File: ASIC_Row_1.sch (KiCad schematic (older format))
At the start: 60 parts, among them U14 BITFURY, U15 BITFURY, U16 BITFURY, U17 BITFURY, U18 BITFURY

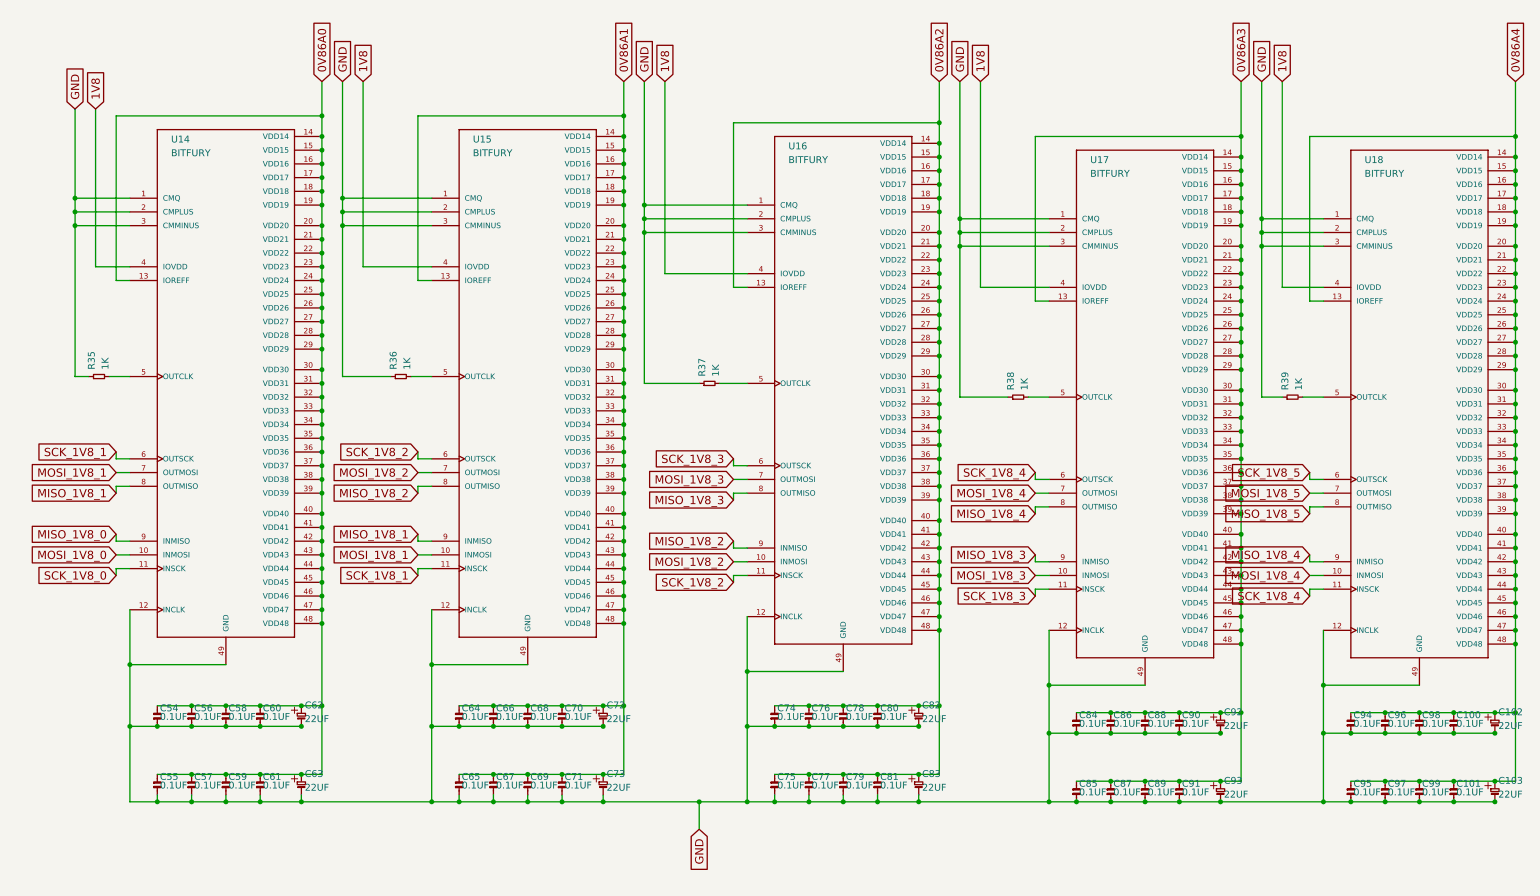
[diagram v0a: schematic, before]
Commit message: Fixed schematic wiring mismatch. initial layout and wiring
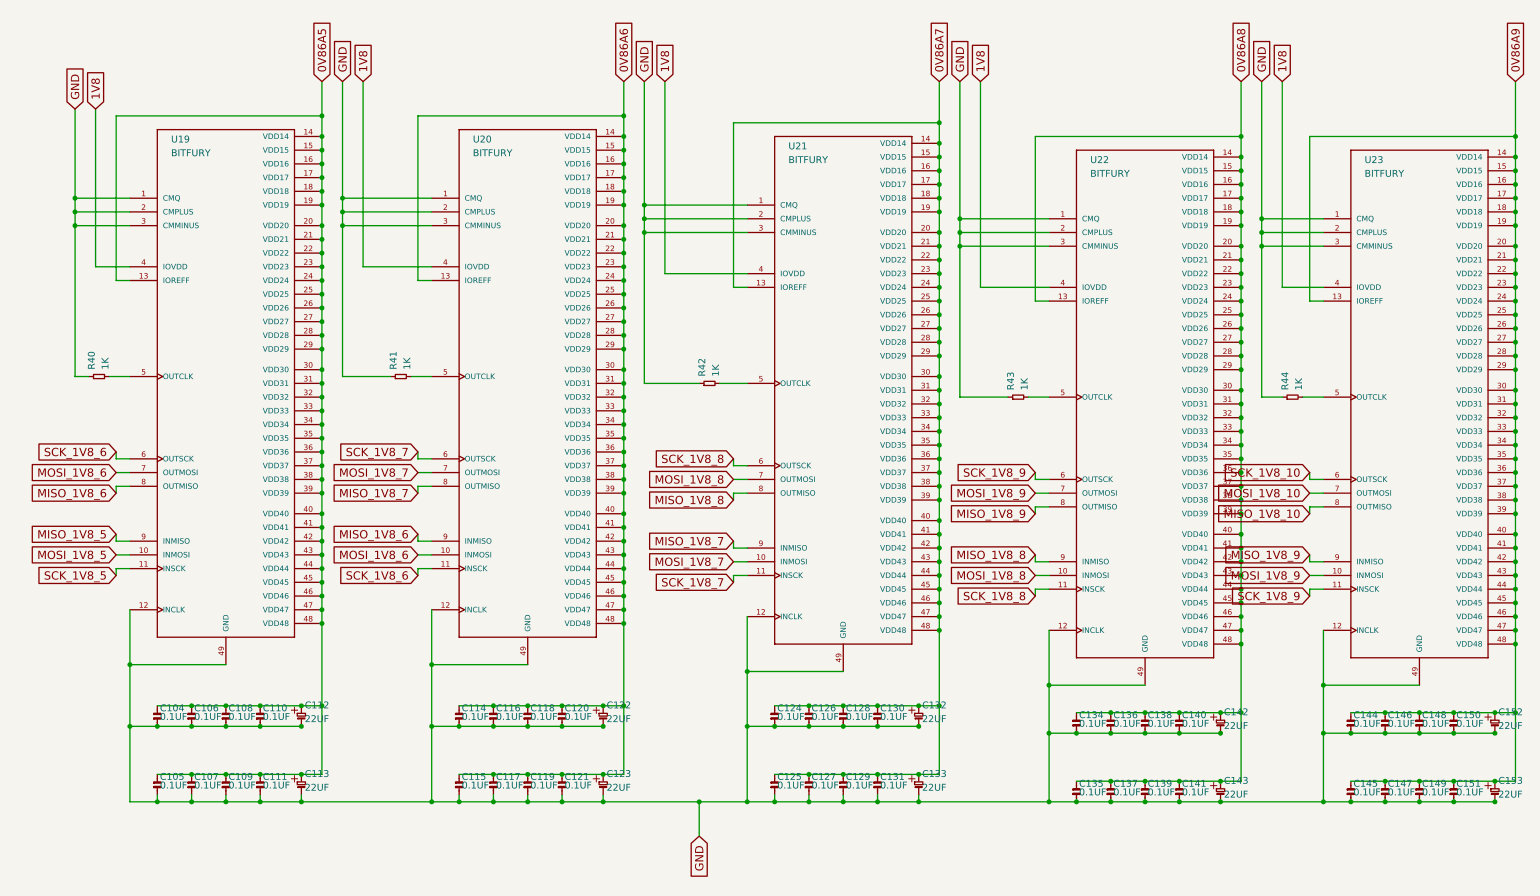
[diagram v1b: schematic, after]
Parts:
- removed C100, C101, C54, C55, C56, C57, C58, C59, C60, C61, C64, C65, C66, C67, C68, C69, C70, C71, C74, C75, C76, C77, C78, C79, C80, C81, C84, C85, C86, C87, C88, C89, C90, C91, C94, C95, C96, C97, C98, C99: 0.1UF, symbol CAPACITOR-NONPOLAR
- removed C102, C103, C62, C63, C72, C73, C82, C83, C92, C93: 22UF, ~, symbol CAPACITOR-POLAR
- removed R35, R36, R37, R38, R39: 1K, symbol RESISTOR
- removed U14, U15, U16, U17, U18: BITFURY, bitfury-QFN48, symbol BITFURY
- added C104, C105, C106, C107, C108, C109, C110, C111, C114, C115, C116, C117, C118, C119, C120, C121, C124, C125, C126, C127, C128, C129, C130, C131, C134, C135, C136, C137, C138, C139, C140, C141, C144, C145, C146, C147, C148, C149, C150, C151: 0.1UF, symbol CAPACITOR-NONPOLAR
- added C112, C113, C122, C123, C132, C133, C142, C143, C152, C153: 22UF, ~, symbol CAPACITOR-POLAR
- added R40, R41, R42, R43, R44: 1K, symbol RESISTOR
- added U19, U20, U21, U22, U23: BITFURY, bitfury-QFN48, symbol BITFURY
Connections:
- net 1V8: now also U19.4 (IOVDD), U20.4 (IOVDD), U21.4 (IOVDD), U22.4 (IOVDD), U23.4 (IOVDD)
- net GND: now also C104.2, C105.2, C106.2, C107.2, C108.2, C109.2, C110.2, C111.2, C112.2, C113.2, C114.2, C115.2, C116.2, C117.2, C118.2, C119.2, C120.2, C121.2, C122.2, C123.2, C124.2, C125.2, C126.2, C127.2, C128.2, C129.2, C130.2, C131.2, C132.2, C133.2, C134.2, C135.2, C136.2, C137.2, C138.2, C139.2, C140.2, C141.2, C142.2, C143.2, C144.2, C145.2, C146.2, C147.2, C148.2, C149.2, C150.2, C151.2, C152.2, C153.2, R40.2, R41.2, R42.2, R43.2, R44.2, U19.1 (CMQ), U19.12 (INCLK), U19.2 (CMPLUS), U19.3 (CMMINUS), U19.49 (GND), U20.1 (CMQ), U20.12 (INCLK), U20.2 (CMPLUS), U20.3 (CMMINUS), U20.49 (GND), U21.1 (CMQ), U21.12 (INCLK), U21.2 (CMPLUS), U21.3 (CMMINUS), U21.49 (GND), U22.1 (CMQ), U22.12 (INCLK), U22.2 (CMPLUS), U22.3 (CMMINUS), U22.49 (GND), U23.1 (CMQ), U23.12 (INCLK), U23.2 (CMPLUS), U23.3 (CMMINUS), U23.49 (GND)
- net MISO_1V8_5: now also U19.9 (INMISO)
- net MOSI_1V8_5: now also U19.10 (INMOSI)
- net SCK_1V8_5: now also U19.11 (INSCK)
- new net: R40.1, U19.5 (OUTCLK)
- new net: R43.1, U22.5 (OUTCLK)
- new net: R44.1, U23.5 (OUTCLK)
- new net: R41.1, U20.5 (OUTCLK)
- new net: R42.1, U21.5 (OUTCLK)
- new net 0V86A5: C104.1, C105.1, C106.1, C107.1, C108.1, C109.1, C110.1, C111.1, C112.1, C113.1, U19.13 (IOREFF), U19.14 (VDD14), U19.15 (VDD15), U19.16 (VDD16), U19.17 (VDD17), U19.18 (VDD18), U19.19 (VDD19), U19.20 (VDD20), U19.21 (VDD21), U19.22 (VDD22), U19.23 (VDD23), U19.24 (VDD24), U19.25 (VDD25), U19.26 (VDD26), U19.27 (VDD27), U19.28 (VDD28), U19.29 (VDD29), U19.30 (VDD30), U19.31 (VDD31), U19.32 (VDD32), U19.33 (VDD33), U19.34 (VDD34), U19.35 (VDD35), U19.36 (VDD36), U19.37 (VDD37), U19.38 (VDD38), U19.39 (VDD39), U19.40 (VDD40), U19.41 (VDD41), U19.42 (VDD42), U19.43 (VDD43), U19.44 (VDD44), U19.45 (VDD45), U19.46 (VDD46), U19.47 (VDD47), U19.48 (VDD48)
- new net 0V86A6: C114.1, C115.1, C116.1, C117.1, C118.1, C119.1, C120.1, C121.1, C122.1, C123.1, U20.13 (IOREFF), U20.14 (VDD14), U20.15 (VDD15), U20.16 (VDD16), U20.17 (VDD17), U20.18 (VDD18), U20.19 (VDD19), U20.20 (VDD20), U20.21 (VDD21), U20.22 (VDD22), U20.23 (VDD23), U20.24 (VDD24), U20.25 (VDD25), U20.26 (VDD26), U20.27 (VDD27), U20.28 (VDD28), U20.29 (VDD29), U20.30 (VDD30), U20.31 (VDD31), U20.32 (VDD32), U20.33 (VDD33), U20.34 (VDD34), U20.35 (VDD35), U20.36 (VDD36), U20.37 (VDD37), U20.38 (VDD38), U20.39 (VDD39), U20.40 (VDD40), U20.41 (VDD41), U20.42 (VDD42), U20.43 (VDD43), U20.44 (VDD44), U20.45 (VDD45), U20.46 (VDD46), U20.47 (VDD47), U20.48 (VDD48)
- new net 0V86A7: C124.1, C125.1, C126.1, C127.1, C128.1, C129.1, C130.1, C131.1, C132.1, C133.1, U21.13 (IOREFF), U21.14 (VDD14), U21.15 (VDD15), U21.16 (VDD16), U21.17 (VDD17), U21.18 (VDD18), U21.19 (VDD19), U21.20 (VDD20), U21.21 (VDD21), U21.22 (VDD22), U21.23 (VDD23), U21.24 (VDD24), U21.25 (VDD25), U21.26 (VDD26), U21.27 (VDD27), U21.28 (VDD28), U21.29 (VDD29), U21.30 (VDD30), U21.31 (VDD31), U21.32 (VDD32), U21.33 (VDD33), U21.34 (VDD34), U21.35 (VDD35), U21.36 (VDD36), U21.37 (VDD37), U21.38 (VDD38), U21.39 (VDD39), U21.40 (VDD40), U21.41 (VDD41), U21.42 (VDD42), U21.43 (VDD43), U21.44 (VDD44), U21.45 (VDD45), U21.46 (VDD46), U21.47 (VDD47), U21.48 (VDD48)
- new net 0V86A8: C134.1, C135.1, C136.1, C137.1, C138.1, C139.1, C140.1, C141.1, C142.1, C143.1, U22.13 (IOREFF), U22.14 (VDD14), U22.15 (VDD15), U22.16 (VDD16), U22.17 (VDD17), U22.18 (VDD18), U22.19 (VDD19), U22.20 (VDD20), U22.21 (VDD21), U22.22 (VDD22), U22.23 (VDD23), U22.24 (VDD24), U22.25 (VDD25), U22.26 (VDD26), U22.27 (VDD27), U22.28 (VDD28), U22.29 (VDD29), U22.30 (VDD30), U22.31 (VDD31), U22.32 (VDD32), U22.33 (VDD33), U22.34 (VDD34), U22.35 (VDD35), U22.36 (VDD36), U22.37 (VDD37), U22.38 (VDD38), U22.39 (VDD39), U22.40 (VDD40), U22.41 (VDD41), U22.42 (VDD42), U22.43 (VDD43), U22.44 (VDD44), U22.45 (VDD45), U22.46 (VDD46), U22.47 (VDD47), U22.48 (VDD48)
- new net 0V86A9: C144.1, C145.1, C146.1, C147.1, C148.1, C149.1, C150.1, C151.1, C152.1, C153.1, U23.13 (IOREFF), U23.14 (VDD14), U23.15 (VDD15), U23.16 (VDD16), U23.17 (VDD17), U23.18 (VDD18), U23.19 (VDD19), U23.20 (VDD20), U23.21 (VDD21), U23.22 (VDD22), U23.23 (VDD23), U23.24 (VDD24), U23.25 (VDD25), U23.26 (VDD26), U23.27 (VDD27), U23.28 (VDD28), U23.29 (VDD29), U23.30 (VDD30), U23.31 (VDD31), U23.32 (VDD32), U23.33 (VDD33), U23.34 (VDD34), U23.35 (VDD35), U23.36 (VDD36), U23.37 (VDD37), U23.38 (VDD38), U23.39 (VDD39), U23.40 (VDD40), U23.41 (VDD41), U23.42 (VDD42), U23.43 (VDD43), U23.44 (VDD44), U23.45 (VDD45), U23.46 (VDD46), U23.47 (VDD47), U23.48 (VDD48)
- new net MISO_1V8_10: U23.8 (OUTMISO)
- new net MISO_1V8_6: U19.8 (OUTMISO), U20.9 (INMISO)
- new net MISO_1V8_7: U20.8 (OUTMISO), U21.9 (INMISO)
- new net MISO_1V8_8: U21.8 (OUTMISO), U22.9 (INMISO)
- new net MISO_1V8_9: U22.8 (OUTMISO), U23.9 (INMISO)
- new net MOSI_1V8_10: U23.7 (OUTMOSI)
- new net MOSI_1V8_6: U19.7 (OUTMOSI), U20.10 (INMOSI)
- new net MOSI_1V8_7: U20.7 (OUTMOSI), U21.10 (INMOSI)
- new net MOSI_1V8_8: U21.7 (OUTMOSI), U22.10 (INMOSI)
- new net MOSI_1V8_9: U22.7 (OUTMOSI), U23.10 (INMOSI)
- new net SCK_1V8_10: U23.6 (OUTSCK)
- new net SCK_1V8_6: U19.6 (OUTSCK), U20.11 (INSCK)
- new net SCK_1V8_7: U20.6 (OUTSCK), U21.11 (INSCK)
- new net SCK_1V8_8: U21.6 (OUTSCK), U22.11 (INSCK)
- new net SCK_1V8_9: U22.6 (OUTSCK), U23.11 (INSCK)
